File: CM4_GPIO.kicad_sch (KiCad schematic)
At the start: 18 parts, among them J1 Conn_01x02_Male, U1 TPD4EUSB30, U2 TPD4EUSB30, U3 MagJack-A70-112-331N126, U5 74LVC1G07SE-7

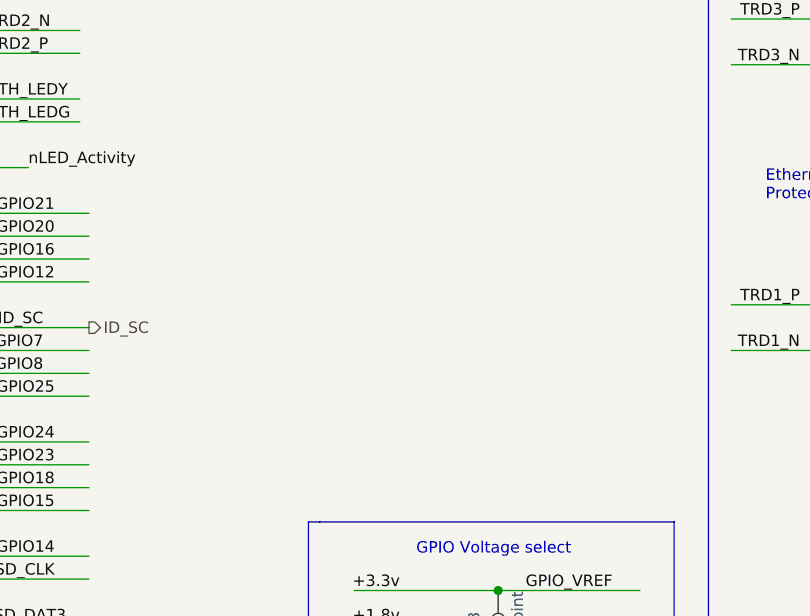
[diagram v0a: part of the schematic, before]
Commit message: Add TODO & SK6812 LED
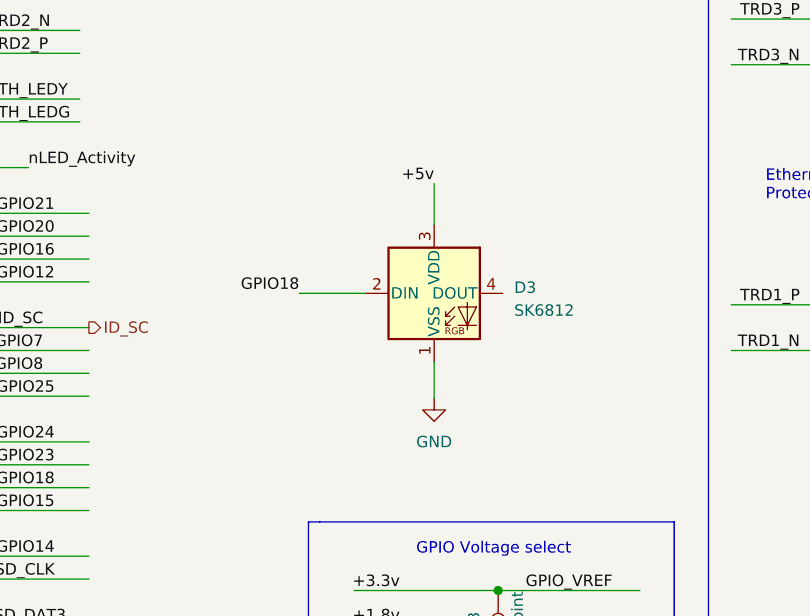
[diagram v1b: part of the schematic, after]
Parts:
- added D3: SK6812, LED_SMD:LED_SK6812_PLCC4_5.0x5.0mm_P3.2mm, symbol LED:SK6812
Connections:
- net +5v: now also D3.3 (VDD)
- net GND: now also D3.1 (VSS)
- net GPIO18: now also D3.2 (DIN)
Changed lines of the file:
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@@
+    (stroke (width 0) (type solid) (color 0 0 0 0))
+  )
+  (wire (pts (xy 137.414 58.42) (xy 144.78 58.42))
     (stroke (width 0) (type solid) (color 0 0 0 0))
   )
@@
   )
   (wire (pts (xy 143.51 95.25) (xy 152.4 95.25))
+    (stroke (width 0) (type solid) (color 0 0 0 0))
+  )
+  (wire (pts (xy 152.4 46.228) (xy 152.4 50.8))
+    (stroke (width 0) (type solid) (color 0 0 0 0))
+  )
+  (wire (pts (xy 152.4 66.04) (xy 152.4 70.104))
     (stroke (width 0) (type solid) (color 0 0 0 0))
   )
@@
     (effects (font (size 1.27 1.27)) (justify right bottom))
   )
+  (label "GPIO18" (at 137.414 58.42 180)
+    (effects (font (size 1.27 1.27)) (justify right bottom))
+  )
   (label "+3.3v" (at 148.59 91.44 180)
     (effects (font (size 1.27 1.27)) (justify right bottom))
   )
   (label "+1.8v" (at 148.59 95.25 180)
+    (effects (font (size 1.27 1.27)) (justify right bottom))
+  )
+  (label "+5v" (at 152.4 46.228 180)
     (effects (font (size 1.27 1.27)) (justify right bottom))
   )
@@
     )
     (property "Datasheet" "" (id 3) (at 101.346 148.59 0)
+      (effects (font (size 1.27 1.27)) hide)
+    )
+    (pin "1")
+  )
+  (symbol (lib_id "power:GND") (at 152.4 70.104 0) (unit 1)
+    (in_bom yes) (on_board yes) (fields_autoplaced)
+    (property "Reference" "#PWR0106" (id 0) (at 152.4 76.454 0)
+      (effects (font (size 1.27 1.27)) hide)
+    )
+    (property "Value" "GND" (id 1) (at 152.4 74.93 0))
+    (property "Footprint" "" (id 2) (at 152.4 70.104 0)
+      (effects (font (size 1.27 1.27)) hide)
+    )
+    (property "Datasheet" "" (id 3) (at 152.4 70.104 0)
       (effects (font (size 1.27 1.27)) hide)
     )
@@
     (pin "5")
   )
+  (symbol (lib_id "LED:SK6812") (at 152.4 58.42 0) (unit 1)
+    (in_bom yes) (on_board yes) (fields_autoplaced)
+    (property "Reference" "D3" (id 0) (at 161.29 57.7849 0)
+      (effects (font (size 1.27 1.27)) (justify left))
+    )
+    (property "Value" "SK6812" (id 1) (at 161.29 60.3249 0)
+      (effects (font (size 1.27 1.27)) (justify left))
+    )
+    (property "Footprint" "LED_SMD:LED_SK6812_PLCC4_5.0x5.0mm_P3.2mm" (id 2) (at 153.67 66.04 0)
+      (effects (font (size 1.27 1.27)) (justify left top) hide)
+    )
+    (property "Datasheet" "https://cdn-shop.adafruit.com/product-files/1138/SK6812+LED+datasheet+.pdf" (id 3) (at 154.94 67.945 0)
+      (effects (font (size 1.27 1.27)) (justify left top) hide)
+    )
+    (pin "1")
+    (pin "2")
+    (pin "3")
+    (pin "4")
+  )
   (symbol (lib_id "CM4IO:TPD4EUSB30") (at 207.01 30.48 0) (unit 1)
